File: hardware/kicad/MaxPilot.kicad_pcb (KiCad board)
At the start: 2 copper layers, 99.1 x 38.1 mm, 12 parts, among them J1 Conn_01x03, U1 WeMos_D1_mini, U2 MOC3041M, U3 MOC3041M

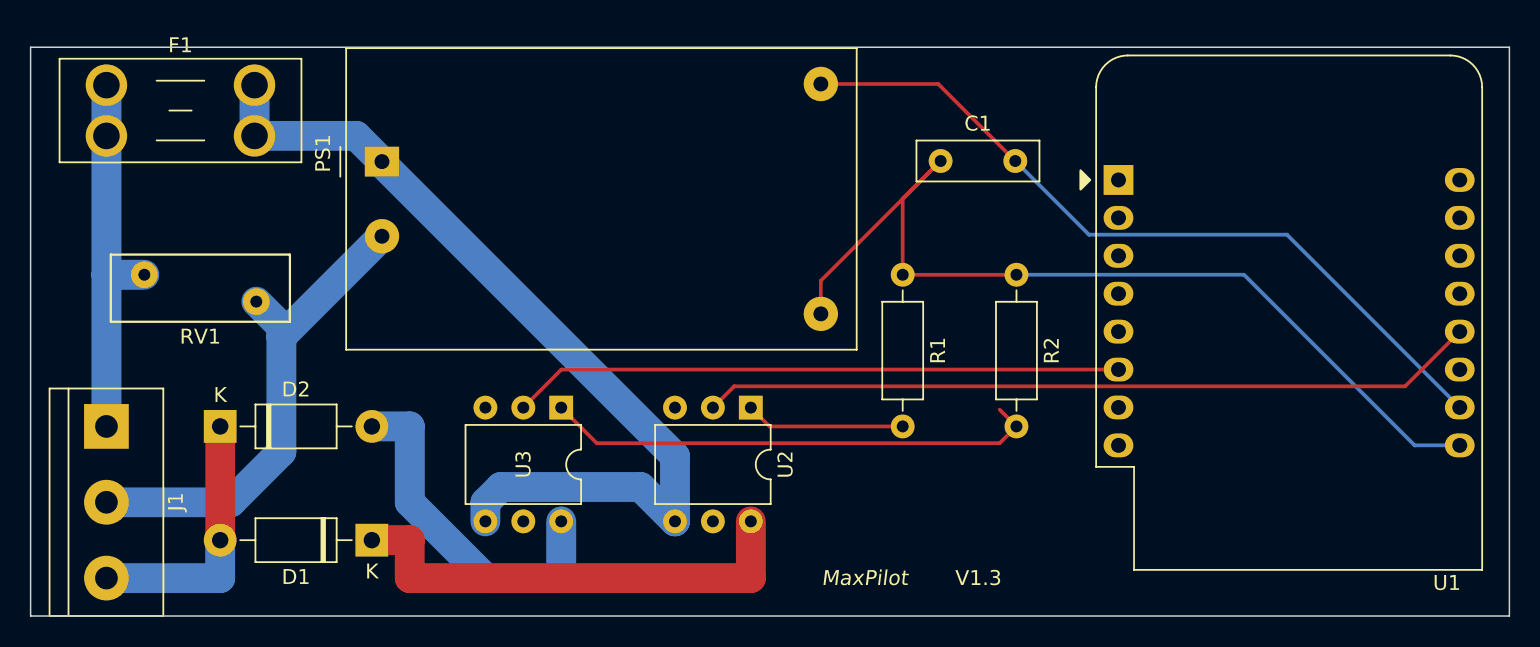
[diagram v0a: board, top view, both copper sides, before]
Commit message: PCB v2.0: redesign for IPC-2221B/IEC 62368-1 mains safety compliance
- Replace J1 terminal block with 7.62mm pitch (was 5.08mm)
- Add IPC-2221B/IEC 62368-1 DRC rules (clearance ≥3.0mm mains↔LV,
  ≥2.5mm mains↔mains, creepage ≥5.0mm) in MaxPilot.kicad_dru
- Add MOC3041M_DIP6_W7.62mm_NC5 footprint: pin 5 (TRIAC substrate,
  DO NOT CONNECT) replaced with NPTH mechanical hole
- Assign mains nets to Line netclass (LINE, NEUT, LINE_P,
  Net-(D1-K), Net-(D2-A)); mains traces at 2mm width
- Re-route PCB to satisfy safety clearances (DRC: 0 errors)
- Update README: BOM, safety section, v2 changelog
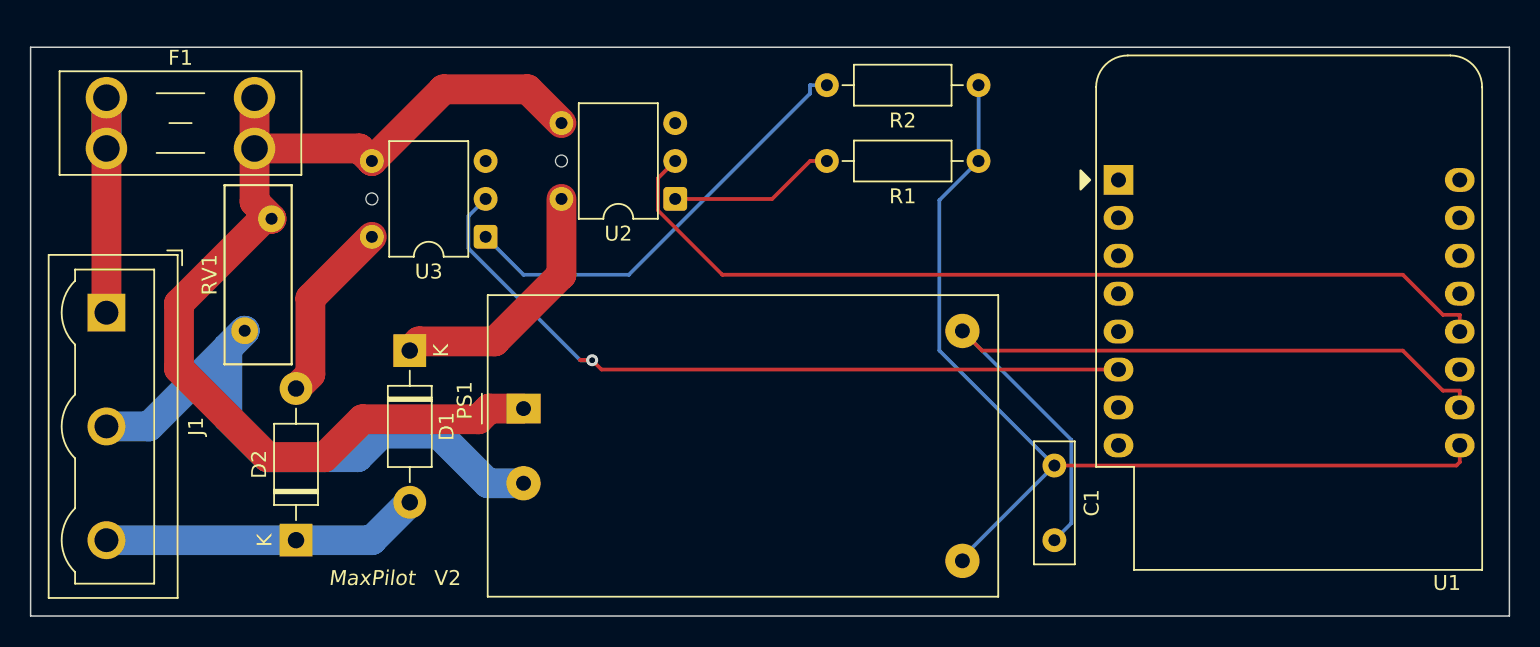
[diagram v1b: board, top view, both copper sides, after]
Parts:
- J1: footprint TerminalBlock:TerminalBlock_bornier-3_P5.08mm -> MaxPilot:TerminalBlock_Generic_1x03_P7.62mm_Horizontal
- U2, U3: footprint Package_DIP:DIP-6_W7.62mm -> MaxPilot:MOC3041M_DIP6_W7.62mm_NC5
- moved C1 21.8 mm to (81.3, 40.7), turned to -90 degrees
- moved PS1 19.1 mm to (45.7, 36.9)
- moved U2 14.9 mm to (55.9, 22.9), turned to 180 degrees
- moved R2 13.0 mm to (76.2, 15.2), turned to 180 degrees
- moved D1 13.0 mm to (38.1, 33.0), turned to -90 degrees
- moved U3 12.5 mm to (43.2, 25.4), turned to 180 degrees
- moved RV1 9.31 mm to (28.8, 24.2), turned to -90 degrees
- moved D2 9.16 mm to (30.5, 45.7), turned to 90 degrees
- moved R1 9.16 mm to (76.2, 20.3), turned to 180 degrees
- moved J1 7.62 mm to (17.8, 30.5)
- moved F1 0.84 mm to (17.8, 16.1)
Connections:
- D2 pad 2: Net-(D2-Pad2) -> Net-(D2-A)
- F1 pad 2: Net-(D2-Pad2) -> LINE_P
- PS1 pad 1: Net-(D2-Pad2) -> LINE_P
- RV1 pad 1: LINE -> LINE_P
- U2 pad 4: Net-(D2-Pad2) -> LINE_P
- U3 pad 4: Net-(D2-Pad2) -> LINE_P
- U3 pad 6: Net-(D2-Pad2) -> Net-(D2-A)
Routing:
- net Net-(D2-Pad2): track 83.9 -> 0.00 mm
- net LINE_P: track 0.00 -> 72.2 mm
- net Net-(D1-K): track 31.7 -> 17.3 mm
- net Net-(U1-MOSI/D7): track 40.9 -> 53.9 mm, vias 0 -> 1
- net Net-(D2-A): track 0.00 -> 12.3 mm
- net Net-(U1-D3): track 52.1 -> 61.5 mm
- net NEUT: track 33.4 -> 41.2 mm
- net LINE: track 25.4 -> 17.8 mm
- net Net-(R2-Pad2): track 33.5 -> 29.5 mm
- net /PILOT: track 17.8 -> 21.4 mm
- net +5V: track 64.3 -> 67.1 mm
- net GND: track 51.8 -> 53.6 mm
- net Net-(R1-Pad2): track 10.7 -> 11.2 mm
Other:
- board text added: "V2"
- board text removed: "V1.3"

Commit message: Add CERN-OHL-S v2 license text to PCB back silkscreen
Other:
- board text added: "CERN-OHL-S v2"
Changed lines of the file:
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@@
 		(net 22)
+	)
+	(gr_text "CERN-OHL-S v2"
+		(at 62.23 49.5)
+		(layer "B.SilkS")
+		(effects
+			(font
+				(size 0.8 0.8)
+				(thickness 0.12)
+			)
+			(justify mirror)
+		)
 	)
 	(embedded_fonts no)

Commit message: Move CERN-OHL-S v2 license to front silkscreen; regenerate Gerbers and images
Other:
- board text added: "MaxPilot V2"
- board text removed: "MaxPilot"
- board text removed: "V2"
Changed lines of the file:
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@@
 		(layer "Edge.Cuts")
 	)
-	(gr_text "MaxPilot"
-		(at 35.56 48.26 0)
+	(gr_text "MaxPilot V2"
+		(at 30.48 48.26 0)
 		(layer "F.SilkS")
 		(effects
@@
 		)
 	)
-	(gr_text "V2"
-		(at 40.64 48.26 0)
+	(gr_text "CERN-OHL-S v2"
+		(at 30.48 49.5 0)
 		(layer "F.SilkS")
 		(effects
 			(font
-				(size 1 1)
-				(thickness 0.15)
+				(size 0.8 0.8)
+				(thickness 0.12)
 			)
 		)
@@
 		(net 22)
 	)
-	(gr_text "CERN-OHL-S v2"
-		(at 62.23 49.5)
-		(layer "B.SilkS")
-		(effects
-			(font
-				(size 0.8 0.8)
-				(thickness 0.12)
-			)
-			(justify mirror)
-		)
-	)
 	(embedded_fonts no)

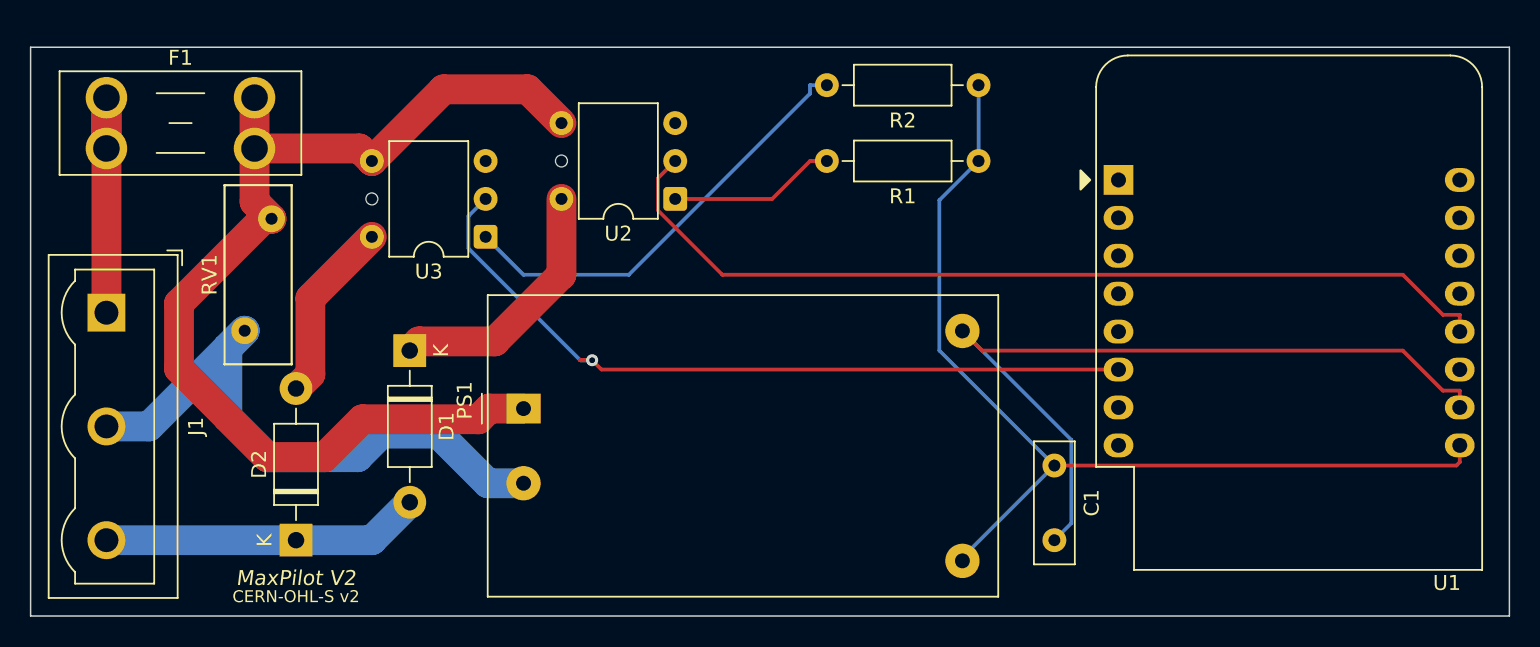
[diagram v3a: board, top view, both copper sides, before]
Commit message: Add M2 mounting holes, reroute PCB, add 3D printable enclosure
- Add 4× M2 mounting holes at corners (H1-H4, annotated)
- Reroute PCB after component repositioning; DRC clean (9 warnings, 0 errors)
- Add hardware/enclosure/MaxPilot_box.scad: OpenSCAD parametric enclosure
  - Base with 4× M2 boss standoffs, friction-fit lid, J1 wire entry cutout
  - Box exterior ~107 × 46 × 36.6 mm, assembly with 4× M2×6 self-tapping screws
- Regenerate Gerbers and PCB images for updated layout
- Switch drill output to single unified .drl file
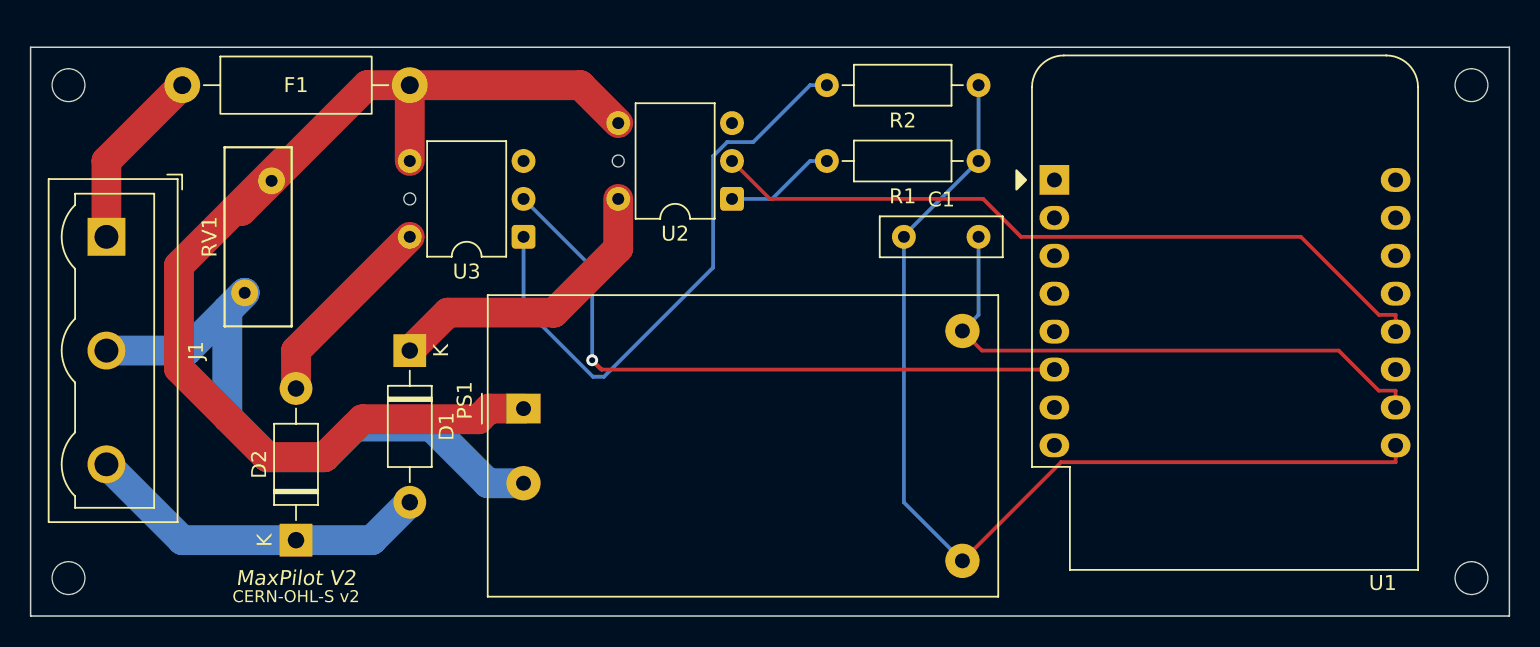
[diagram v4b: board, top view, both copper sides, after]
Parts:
- added H1: MountingHole_2.2mm_M2, MountingHole:MountingHole_2.2mm_M2, F.Cu at (15.2, 15.2)
- added H2: MountingHole_2.2mm_M2, MountingHole:MountingHole_2.2mm_M2, F.Cu at (109.2, 15.2)
- added H3: MountingHole_2.2mm_M2, MountingHole:MountingHole_2.2mm_M2, F.Cu at (15.2, 48.3)
- added H4: MountingHole_2.2mm_M2, MountingHole:MountingHole_2.2mm_M2, F.Cu at (109.2, 48.3)
- F1: footprint Fuse:Fuseholder_Blade_Mini_Keystone_3568 -> Resistor_THT:R_Axial_DIN0411_L9.9mm_D3.6mm_P15.24mm_Horizontal
- moved C1 18.3 mm to (71.2, 25.4), turned to 0 degrees
- moved F1 5.15 mm to (22.9, 15.2)
- moved J1 5.08 mm to (17.8, 25.4)
- moved U1 4.30 mm to (81.3, 21.6)
- moved U2 3.80 mm to (59.7, 22.9)
- moved RV1 2.54 mm to (28.8, 21.6)
- moved U3 2.54 mm to (45.7, 25.4)
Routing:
- net GND: track 53.6 -> 38.6 mm
- net Net-(U1-D3): track 61.5 -> 49.8 mm
- net Net-(R2-Pad2): track 29.5 -> 39.4 mm
- net Net-(U1-MOSI/D7): track 53.9 -> 45.7 mm
- net LINE_P: track 72.2 -> 79.1 mm
- net LINE: track 17.8 -> 12.3 mm
- net Net-(R1-Pad2): track 11.2 -> 7.41 mm
- net Net-(D1-K): track 17.3 -> 20.1 mm
- net /PILOT: track 21.4 -> 23.5 mm
- net NEUT: track 41.2 -> 43.0 mm
- net +5V: track 67.1 -> 68.4 mm
- net Net-(D2-A): track 12.3 -> 13.3 mm
